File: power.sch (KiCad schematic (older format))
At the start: 48 parts

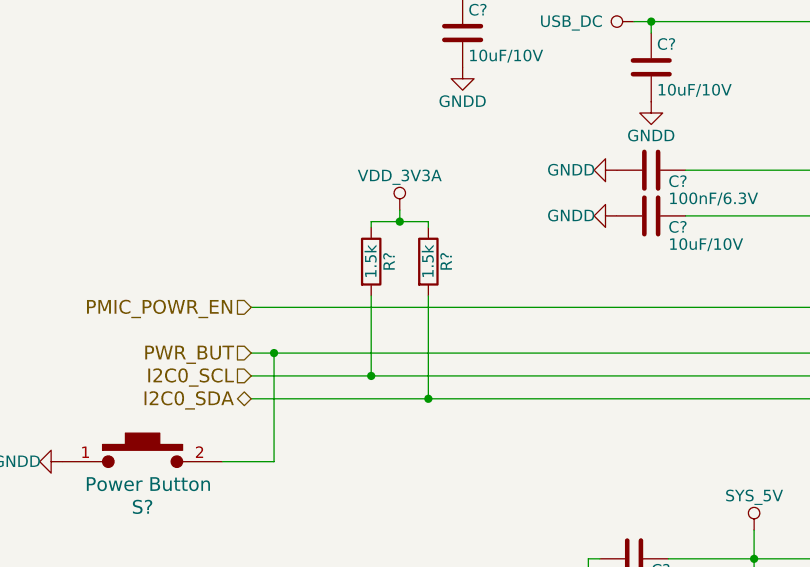
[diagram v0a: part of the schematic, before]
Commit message: gpio and boot config
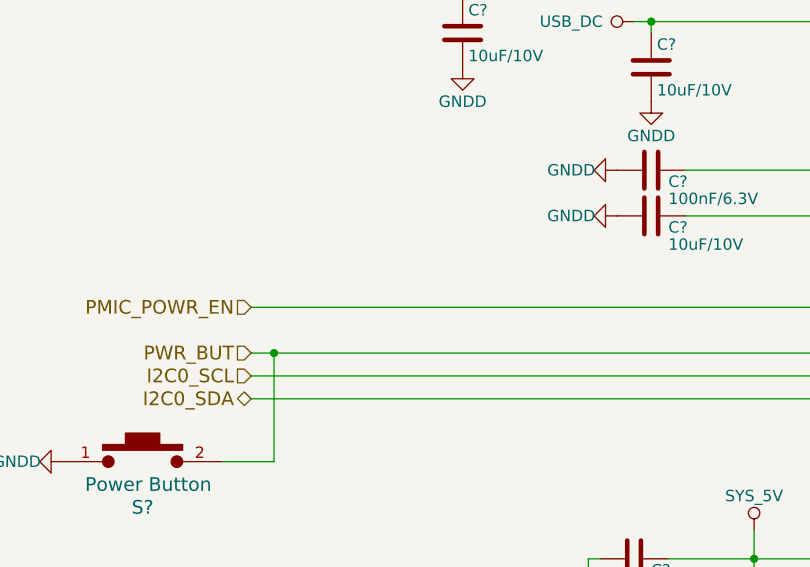
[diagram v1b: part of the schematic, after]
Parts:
- removed R? (x2): 1.5k, symbol R
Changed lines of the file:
@@
 $Descr A4 11693 8268
 encoding utf-8
-Sheet 2 9
+Sheet 2 10
 Title ""
 Date ""
@@
 	0    1    1    0
 $EndComp
-$Comp
-L R R?
-U 1 1 589DF352
-P 3250 2050
-F 0 "R?" V 3330 2050 50  0000 C CNN
-F 1 "1.5k" V 3250 2050 50  0000 C CNN
-F 2 "" V 3180 2050 50  0000 C CNN
-F 3 "" H 3250 2050 50  0000 C CNN
-	1    3250 2050
-	1    0    0    -1
-$EndComp
 Text HLabel 2475 2550 0    60   Input ~ 0
 I2C0_SCL
 Text HLabel 2475 2650 0    60   BiDi ~ 0
 I2C0_SDA
-$Comp
-L R R?
-U 1 1 589DF4C3
-P 3000 2050
-F 0 "R?" V 3080 2050 50  0000 C CNN
-F 1 "1.5k" V 3000 2050 50  0000 C CNN
-F 2 "" V 2930 2050 50  0000 C CNN
-F 3 "" H 3000 2050 50  0000 C CNN
-	1    3000 2050
-	1    0    0    -1
-$EndComp
-$Comp
-L VDD_3V3A #PWR?
-U 1 1 589DF53D
-P 3125 1825
-F 0 "#PWR?" H 3125 1675 50  0001 C CNN
-F 1 "VDD_3V3A" H 3125 1975 50  0000 C CNN
-F 2 "" H 3125 1825 50  0000 C CNN
-F 3 "" H 3125 1825 50  0000 C CNN
-	1    3125 1825
-	1    0    0    -1
-$EndComp
 $Comp
 L C C?
@@
 	2475 2650 5025 2650
 Wire Wire Line
-	3000 1900 3000 1875
-Wire Wire Line
-	3000 1875 3250 1875
-Wire Wire Line
-	3250 1875 3250 1900
-Wire Wire Line
-	3125 1825 3125 1875
-Connection ~ 3125 1875
-Wire Wire Line
-	3000 2200 3000 2550
-Connection ~ 3000 2550
-Wire Wire Line
-	3250 2200 3250 2650
-Connection ~ 3250 2650
-Wire Wire Line
 	4300 3350 5025 3350

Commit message: gpio assignment done
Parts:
- gave numbers to parts that had none: 1
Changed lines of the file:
@@
 $EndDescr
 $Comp
-L TPS65217C U?
+L TPS65217C IC?
 U 1 1 589A192D
 P 6125 2950
-F 0 "U?" H 5325 5200 60  0000 C CNN
+F 0 "IC?" H 5325 5200 60  0000 C CNN
 F 1 "TPS65217C" H 6775 5200 60  0000 C CNN
 F 2 "" H 6125 2950 60  0001 C CNN

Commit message: annotation, wip erc
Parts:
- gave numbers to parts that had none: 46

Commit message: wip sys and power
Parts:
- removed C10, C11, C12, C15, C19, C20, C21, C22, C23, C9: 10uF/10V, symbol C
- removed C14: 100nF/6.3V, symbol C
- removed C17, C18: 2.2uF/6.3V, symbol C
- removed D9: LTST-C191TBKT, symbol LED
- removed IC1: TPS65217C, symbol TPS65217C
- removed L2, L3, L4: LQM2HPN2R2MG0L, symbol L
- removed R16: 100k, symbol R
- removed R17, R18, R19, R21: 0R, symbol R
- removed R20: DNP, symbol R
- removed R22: 4.75k, symbol R
- removed S1: Power Button, symbol PushButton
- added C?: 10uF/10V, symbol C
- added IC? (x2): OSD335x, GHI-SoMs-Processors_OSD3358, symbol OSD335x
- added J?: GS2, Connectors:GS2, symbol GS2
- added R? (x2): 1.5k, symbol R
- added R?: 10k, symbol R
- added U?: 24LC32AT-I, TO_SOT_Packages_SMD:SOT-23-5, symbol AT24CS32-STUM
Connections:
- net BAT: now also IC?.Y2 (BAT_1), IC?.Y3 (BAT_2)
- net BAT_SENSE: now also IC?.Y1 (BATT_VOLT)
- net BAT_TS: now also IC?.W1 (BAT_TEMP)
- net GNDD: now also C?.2, U?.2 (GND)
- net I2C0_SCL: now also IC?.C16 (I2C0_SCL), IC?.C20 (PMIC_I2C_SCL), R?.1, U?.1 (SCL)
- net I2C0_SDA: now also IC?.C17 (I2C0_SDA), IC?.C19 (PMIC_I2C_SDA), R?.1, U?.3 (SDA)
- net LDO_PGOOD: now also IC?.B20 (PMIC_LDO_PGOOD)
- net PMIC_INT: now also IC?.B19 (PMIC_INTN)
- net PMIC_PGOOD: now also IC?.A20 (PMIC_PGOOD)
- net PWR_BUT: now also IC?.D20 (PWR_BUT)
- net SYS_5V: now also IC?.W4 (SYS_5V_1), IC?.Y4 (SYS_5V_2)
- net USB_DC: now also IC?.Y8 (VIN_USB_0), IC?.Y9 (VIN_USB_1)
- net VDD_1V8: now also IC?.N16 (VDD_1V8_0), IC?.R16 (VDD_1V8_1)
- net VDD_3V3AUX: now also IC?.Y11 (VDD_3V3AUX)
- net VDD_3V3B: now also C?.1, J?.1 (G1), R?.1, R?.2, R?.2, U?.4 (VCC)
- net VDD_5V: now also IC?.Y5 (VIN_5V_0), IC?.Y6 (VIN_5V_1)
- new net: IC?.C6 (PMIC_POWER_EN), IC?.D19 (PWR_EN)
- new net: IC?.U20 (VDD_3V3B_0), IC?.V20 (VDD_3V3B_1), J?.2 (G2)
- new net: R?.2, U?.5 (WP)
- new net PMIC_nWAKEUP: IC?.A19 (PMIC_WAKEUPN)
- no-connect marks 12 -> 63
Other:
- moved on the sheet: C13, C8

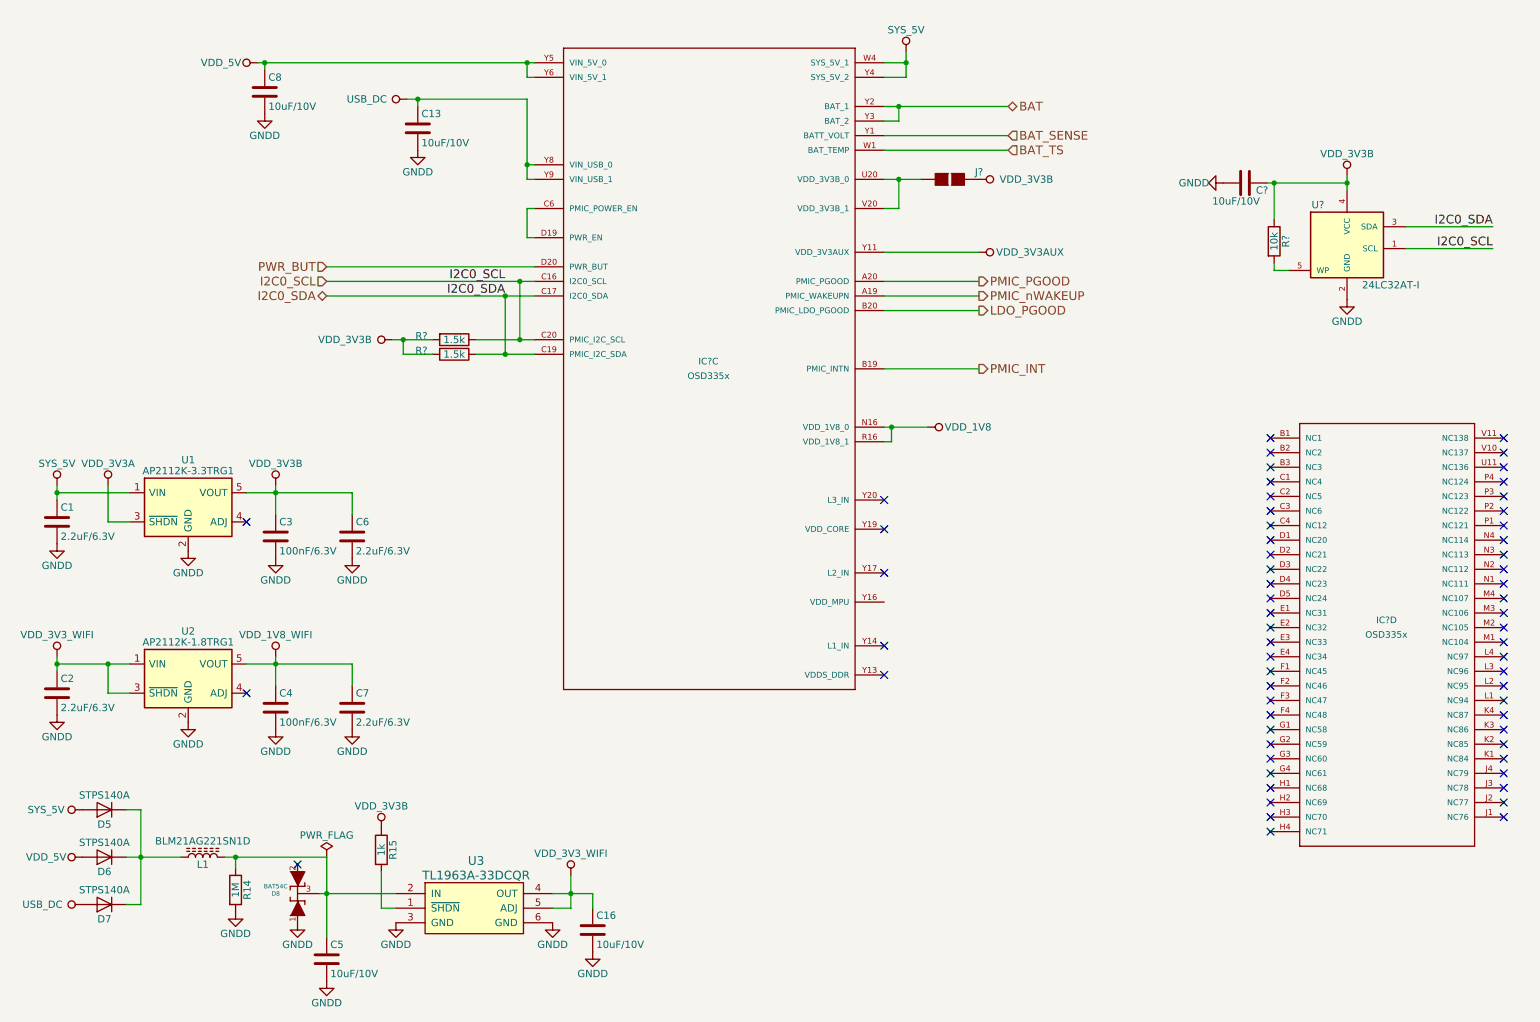
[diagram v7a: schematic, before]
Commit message: only io connectors remaining
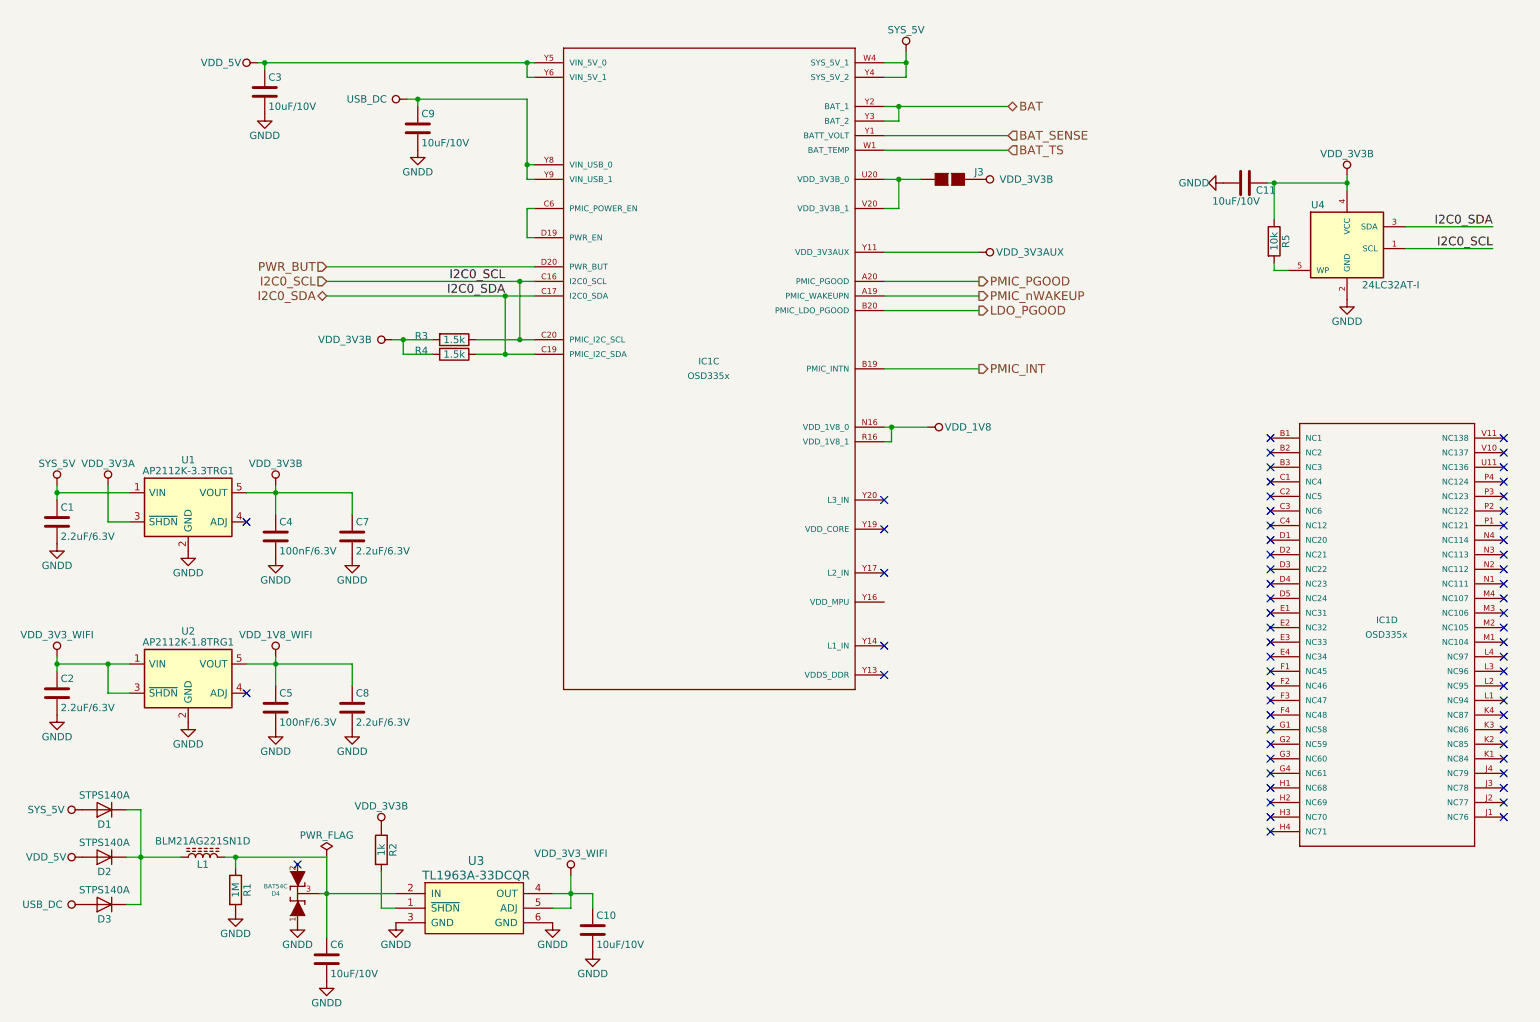
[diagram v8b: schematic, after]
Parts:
- gave numbers to parts that had none: 7
- renumbered C16 to C10, C8 to C3, C3 to C4, C4 to C5, C5 to C6, C6 to C7, C7 to C8, C13 to C9, D5 to D1, D6 to D2, D7 to D3, D8 to D4, R14 to R1, R15 to R2
